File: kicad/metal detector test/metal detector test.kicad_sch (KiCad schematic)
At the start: 107 parts, among them J1 3.5mm audio jack TRS, Q1 PNP, Q2 NPN, SW0 SW_SPST, SW1 SW_SPST, SW2 SW_SPST, SW3 SW_SPST, SW4 SW_SPST, SW5 SW_SPST, SW6 SW_SPST, SW7 SW_SPST, SW8 SW_SPST, SW9 SW_SPST, U1 9v lin reg, U10 3.3v lin reg, U11 lp filter, U12 op amp (lower voltage), U2 op amp (higher voltage), U3 nucleo-32 uC module, U4 5v lin reg, U5 3.3v lin reg, U6 audio amp, U7 lp filter, U8 switch debounce, U9 5v lin reg

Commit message: slow progress
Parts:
- added JP5: SolderJumper_2_Open_big, allen footprints:SolderJumper-2_Open_big_allen, symbol Jumper:SolderJumper_2_Open
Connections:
- net +9V: now also JP5.1 (A); no longer C1.1, R1.1, R2.1, R3.1
- new net: C1.1, JP5.2 (B), R1.1, R2.1, R3.1
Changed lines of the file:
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@@
   (junction (at 30.48 58.42) (diameter 0) (color 0 0 0 0)
   )
+  (junction (at 55.88 20.32) (diameter 0) (color 0 0 0 0)
+  )
   (junction (at 139.7 20.32) (diameter 0) (color 0 0 0 0)
   )
@@
     (stroke (width 0) (type default))
   )
+  (wire (pts (xy 59.69 20.32) (xy 55.88 20.32))
+    (stroke (width 0) (type default))
+  )
   (wire (pts (xy 20.32 78.74) (xy 20.32 81.28))
     (stroke (width 0) (type default))
@@
       (effects (font (size 1.27 1.27)) hide)
     )
-    (property "Datasheet" "https://www.ti.com/lit/gpn/OPA2320" (at 109.22 22.86 0)
+    (property "Datasheet" "https://www.ti.com/lit/ds/symlink/opa2140.pdf?HQS=dis-dk-null-digikeymode-dsf-pf-null-wwe&ts=1680023654676&ref_url=https%253A%252F%252Fwww.ti.com%252Fgeneral%252Fdocs%252Fsuppproductinfo.tsp%253FdistId%253D10%2526gotoUrl%253Dhttps%253A%252F%252Fwww.ti.com%252Flit%252Fgpn%252Fopa2140" (at 109.22 22.86 0)
       (effects (font (size 1.27 1.27)) hide)
     )
@@
       (effects (font (size 1.27 1.27) italic) (justify left) hide)
     )
-    (property "Datasheet" "http://www.st.com/content/ccc/resource/technical/document/datasheet/41/4f/b3/b0/12/d4/47/88/CD00000444.pdf/files/CD00000444.pdf/jcr:content/translations/en.CD00000444.pdf" (at 27.94 110.49 0)
+    (property "Datasheet" "https://www.ti.com/lit/ds/slvs059t/slvs059t.pdf" (at 27.94 110.49 0)
       (effects (font (size 1.27 1.27)) hide)
     )
@@
       (effects (font (size 1.27 1.27)) hide)
     )
-    (property "Datasheet" "https://www.ti.com/lit/gpn/OPA2320" (at 90.17 55.88 0)
+    (property "Datasheet" "https://www.ti.com/lit/ds/symlink/opa2140.pdf?HQS=dis-dk-null-digikeymode-dsf-pf-null-wwe&ts=1680023654676&ref_url=https%253A%252F%252Fwww.ti.com%252Fgeneral%252Fdocs%252Fsuppproductinfo.tsp%253FdistId%253D10%2526gotoUrl%253Dhttps%253A%252F%252Fwww.ti.com%252Flit%252Fgpn%252Fopa2140" (at 90.17 55.88 0)
       (effects (font (size 1.27 1.27)) hide)
     )
@@
     )
   )
-  (symbol (lib_id "power:+9V") (at 45.72 20.32 0) (unit 1)
+  (symbol (lib_id "power:+9V") (at 67.31 20.32 270) (unit 1)
     (in_bom yes) (on_board yes) (dnp no) (fields_autoplaced)
-    (property "Reference" "#PWR01" (at 45.72 24.13 0)
+    (property "Reference" "#PWR01" (at 63.5 20.32 0)
       (effects (font (size 1.27 1.27)) hide)
     )
-    (property "Value" "+9V" (at 45.72 15.24 0)
-      (effects (font (size 1.27 1.27)))
+    (property "Value" "+9V" (at 71.12 20.955 90)
+      (effects (font (size 1.27 1.27)) (justify left))
     )
-    (property "Footprint" "" (at 45.72 20.32 0)
+    (property "Footprint" "" (at 67.31 20.32 0)
       (effects (font (size 1.27 1.27)) hide)
     )
-    (property "Datasheet" "" (at 45.72 20.32 0)
+    (property "Datasheet" "" (at 67.31 20.32 0)
       (effects (font (size 1.27 1.27)) hide)
     )
@@
       (effects (font (size 1.27 1.27) italic) hide)
     )
-    (property "Datasheet" "https://www.analog.com/media/en/technical-documentation/data-sheets/112935ff.pdf" (at 152.4 21.59 0)
+    (property "Datasheet" "https://www.ti.com/lit/ds/symlink/lm2940-n.pdf?HQS=dis-dk-null-digikeymode-dsf-pf-null-wwe&ts=1680023082050&ref_url=https%253A%252F%252Fwww.ti.com%252Fgeneral%252Fdocs%252Fsuppproductinfo.tsp%253FdistId%253D10%2526gotoUrl%253Dhttps%253A%252F%252Fwww.ti.com%252Flit%252Fgpn%252Flm2940-n" (at 152.4 21.59 0)
       (effects (font (size 1.27 1.27)) hide)
     )
@@
     )
   )
+  (symbol (lib_id "Jumper:SolderJumper_2_Open") (at 63.5 20.32 180) (unit 1)
+    (in_bom yes) (on_board yes) (dnp no) (fields_autoplaced)
+    (property "Reference" "JP5" (at 63.5 15.24 0)
+      (effects (font (size 1.27 1.27)))
+    )
+    (property "Value" "SolderJumper_2_Open_big" (at 63.5 17.78 0)
+      (effects (font (size 1.27 1.27)))
+    )
+    (property "Footprint" "allen footprints:SolderJumper-2_Open_big_allen" (at 63.5 20.32 0)
+      (effects (font (size 1.27 1.27)) hide)
+    )
+    (property "Datasheet" "~" (at 63.5 20.32 0)
+      (effects (font (size 1.27 1.27)) hide)
+    )
+    (property "MPN" "" (at 63.5 20.32 0)
+      (effects (font (size 1.27 1.27)) hide)
+    )
+    (pin "1")
+    (pin "2")
+    (instances
+      (project "metal detector test"
+        (path "/aac94249-970f-41d5-8c24-6bade512464d"
+          (reference "JP5") (unit 1)
+        )
+      )
+    )
+  )
   (symbol (lib_id "power:GNDPWR") (at 139.7 25.4 0) (unit 1)
     (in_bom yes) (on_board yes) (dnp no)
@@
       (effects (font (size 1.27 1.27)) hide)
     )
-    (property "Datasheet" "https://www.ti.com/lit/gpn/OPA2320" (at 90.17 55.88 0)
+    (property "Datasheet" "https://www.ti.com/lit/ds/symlink/opa2140.pdf?HQS=dis-dk-null-digikeymode-dsf-pf-null-wwe&ts=1680023654676&ref_url=https%253A%252F%252Fwww.ti.com%252Fgeneral%252Fdocs%252Fsuppproductinfo.tsp%253FdistId%253D10%2526gotoUrl%253Dhttps%253A%252F%252Fwww.ti.com%252Flit%252Fgpn%252Fopa2140" (at 90.17 55.88 0)
       (effects (font (size 1.27 1.27)) hide)
     )
@@
       (effects (font (size 1.27 1.27) italic) (justify left) hide)
     )
-    (property "Datasheet" "http://www.st.com/content/ccc/resource/technical/document/datasheet/41/4f/b3/b0/12/d4/47/88/CD00000444.pdf/files/CD00000444.pdf/jcr:content/translations/en.CD00000444.pdf" (at 27.94 74.93 0)
+    (property "Datasheet" "https://www.ti.com/lit/ds/slvs059t/slvs059t.pdf" (at 27.94 74.93 0)
       (effects (font (size 1.27 1.27)) hide)
     )

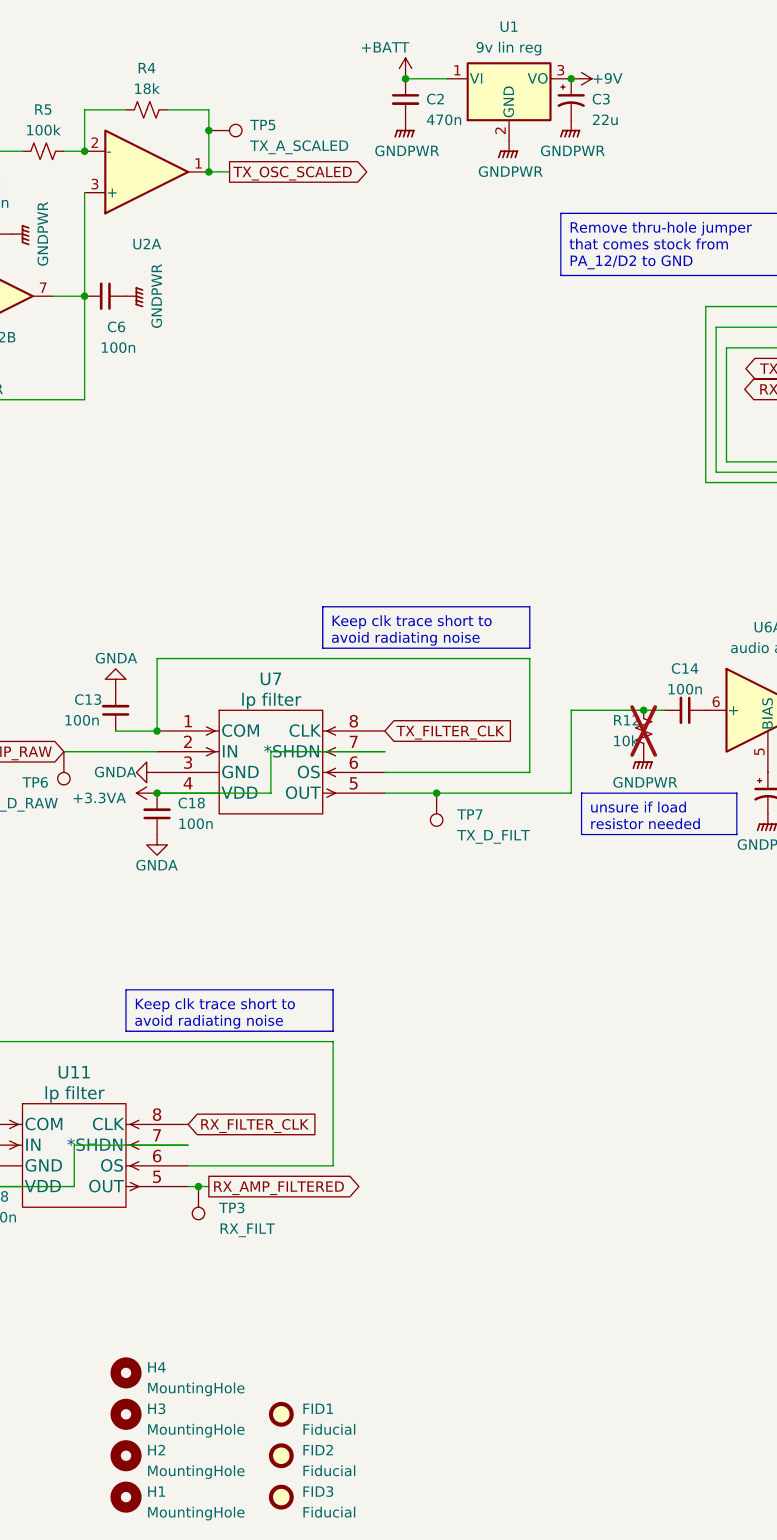
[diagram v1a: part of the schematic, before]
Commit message: Added holes on corners of OLED footprint after carefully measuring twice, working on layout still.
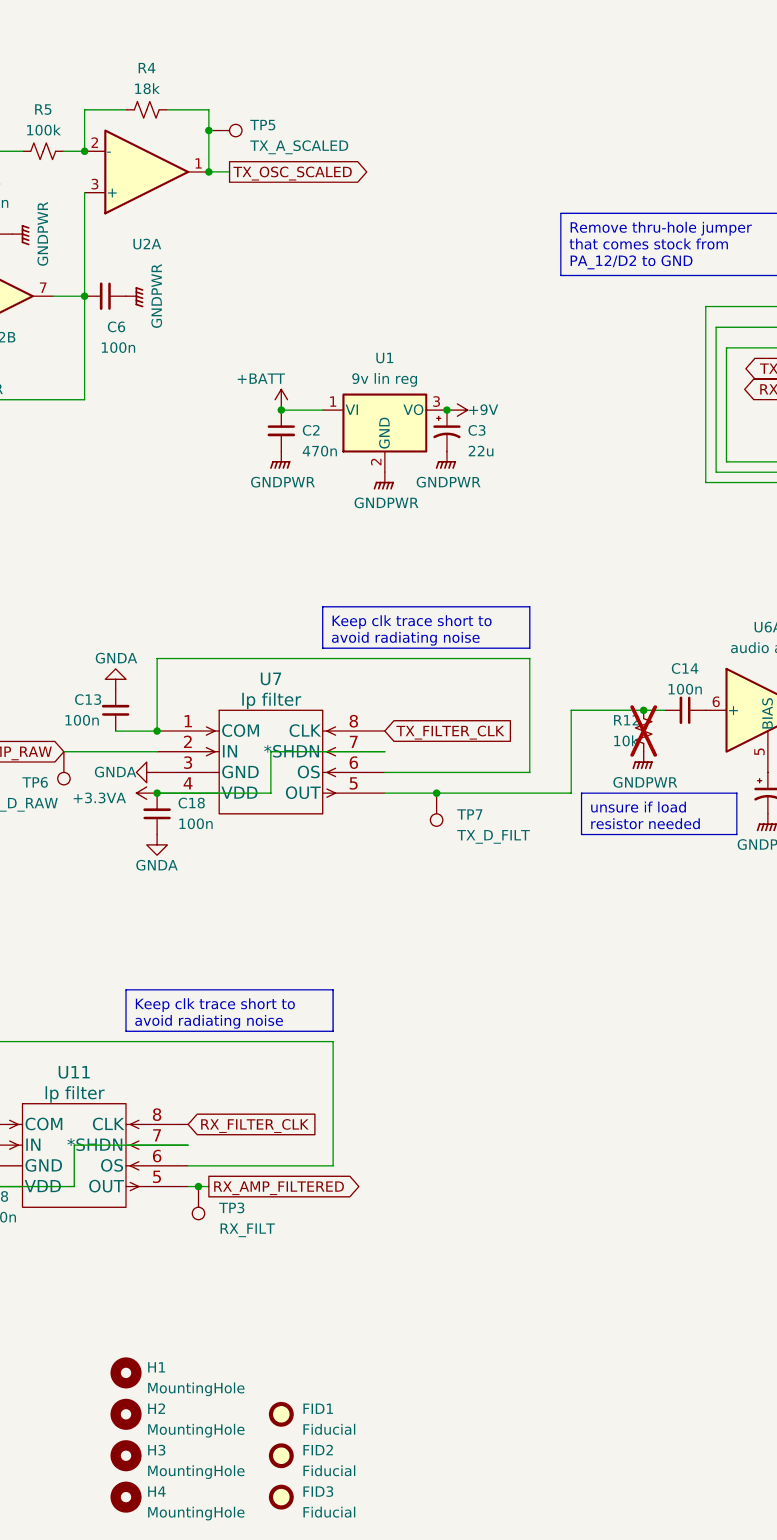
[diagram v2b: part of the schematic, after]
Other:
- moved on the sheet: C2, C3, H1, H2, H3, H4, U1

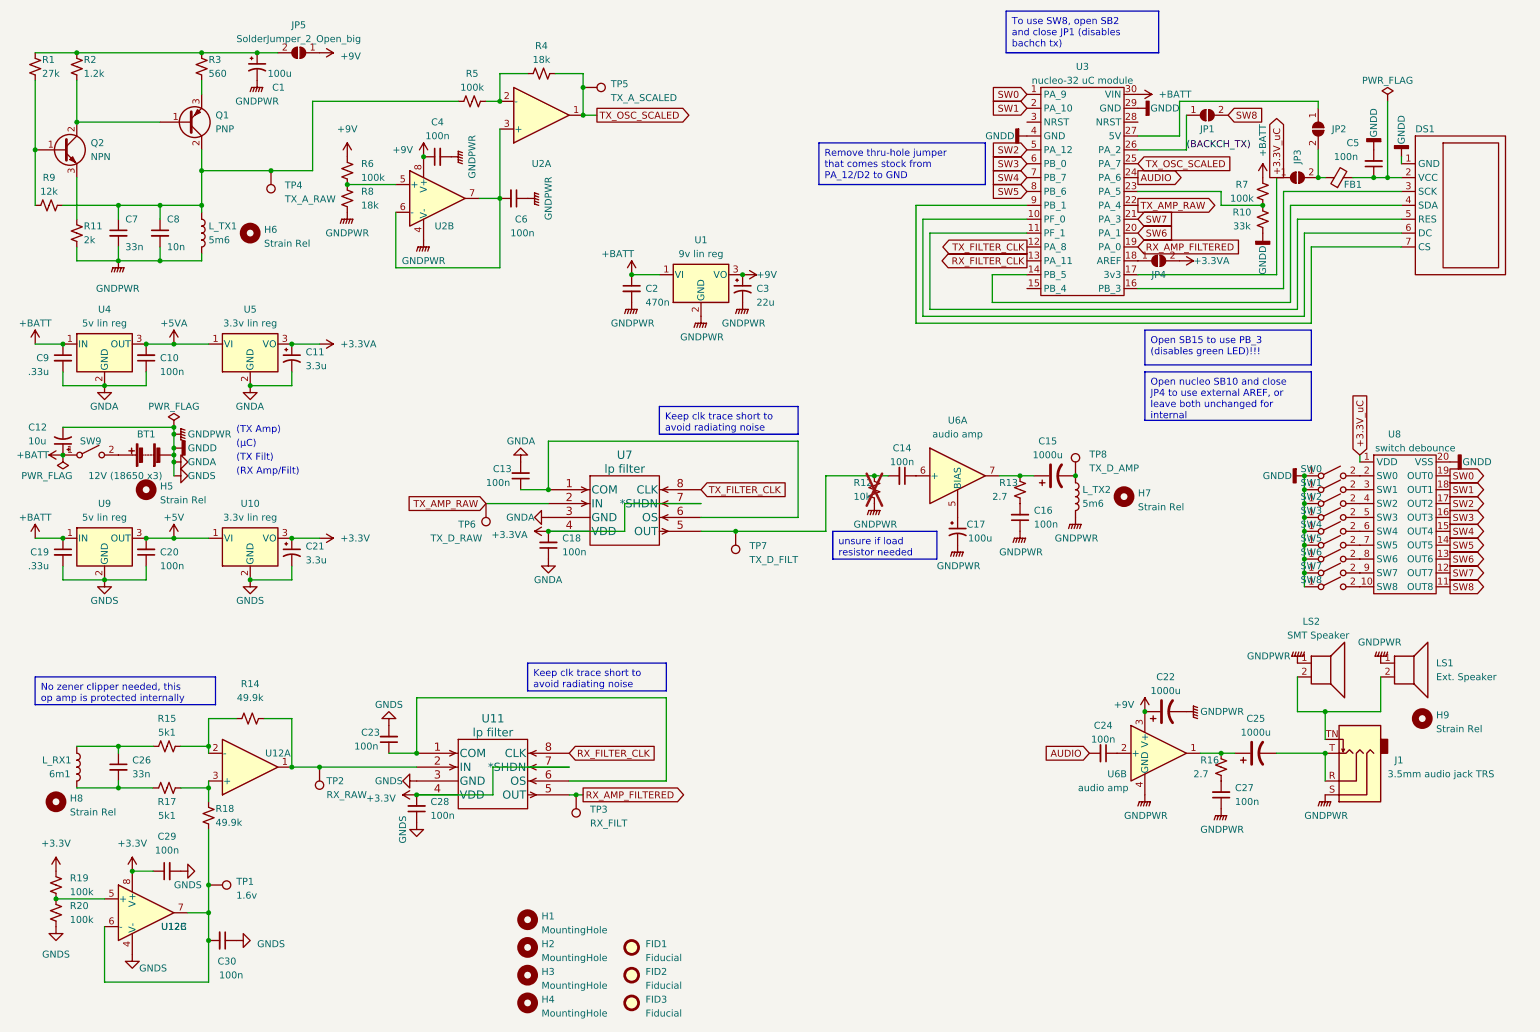
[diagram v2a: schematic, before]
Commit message: Making custom mounting / strain relief holes
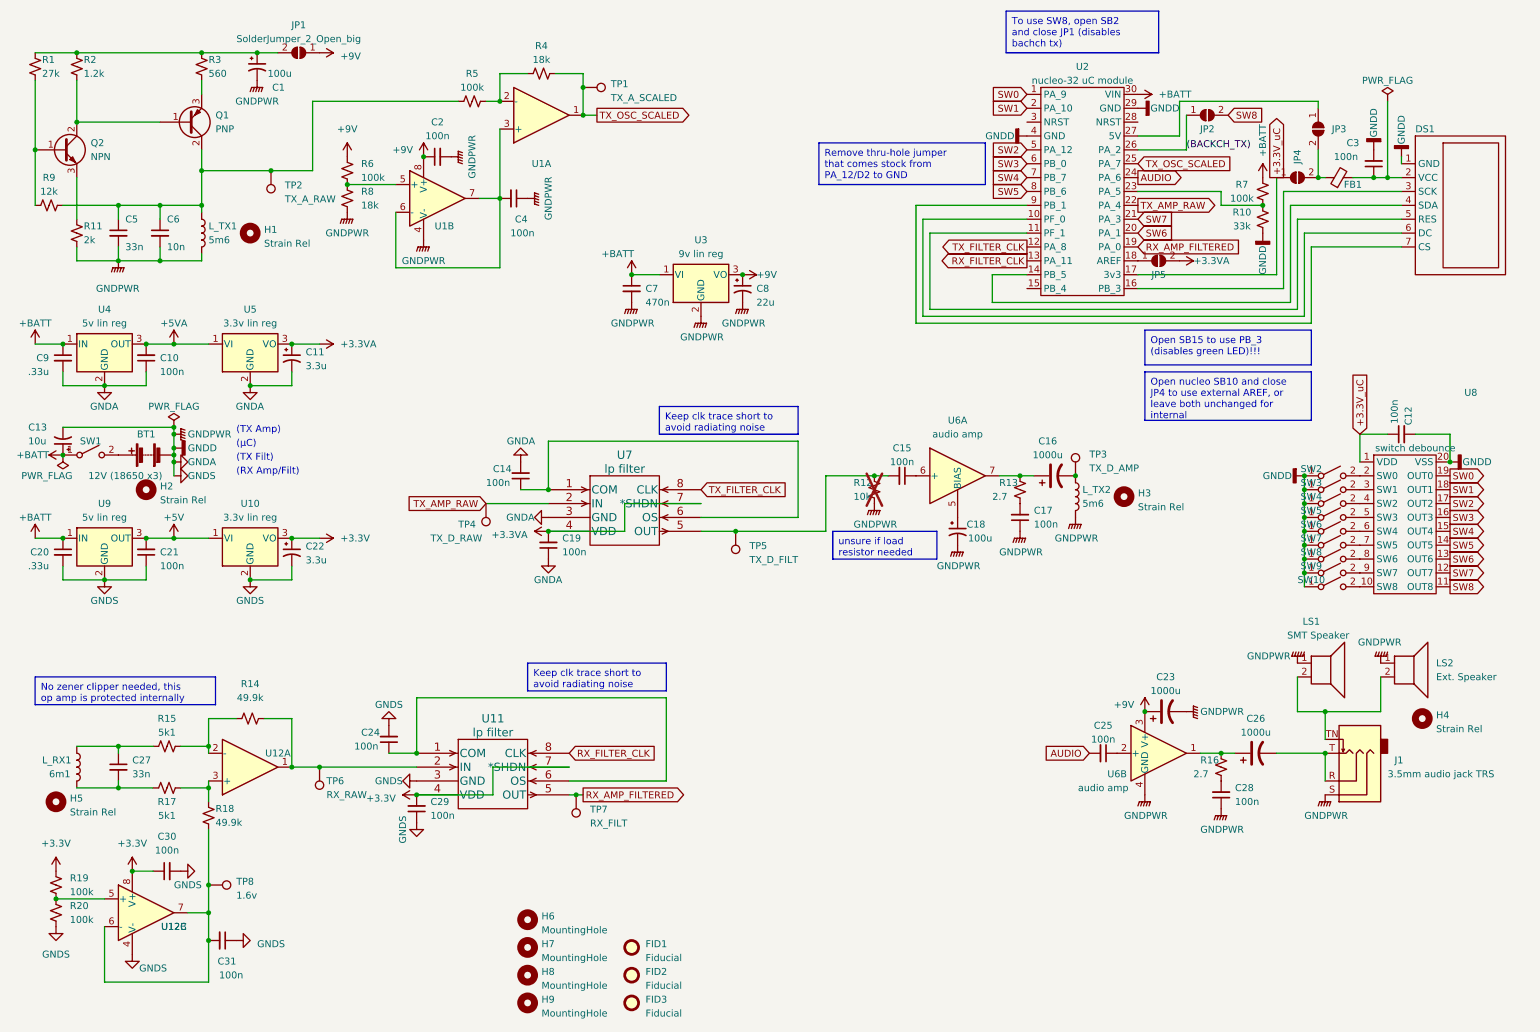
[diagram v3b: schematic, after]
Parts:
- removed H2, H3, H4: MountingHole, MountingHole:MountingHole_3.7mm, symbol Mechanical:MountingHole
- added C12: 100n, Capacitor_SMD:C_0805_2012Metric_Pad1.18x1.45mm_HandSolder, symbol Device:C_Small
- added H7, H8, H9: MountingHole, allen footprints:mounting_hole_4-40_thru, symbol Mechanical:MountingHole
- H1: renamed from H6; footprint MountingHole:MountingHole_3.2mm_M3 -> allen footprints:mounting_hole_3mm
- H2: renamed from H5; footprint MountingHole:MountingHole_3.2mm_M3 -> allen footprints:mounting_hole_3mm
- H3: renamed from H7; footprint MountingHole:MountingHole_3.2mm_M3 -> allen footprints:mounting_hole_3mm
- H4: renamed from H9; footprint MountingHole:MountingHole_3.2mm_M3 -> allen footprints:mounting_hole_3mm
- H5: renamed from H8; footprint MountingHole:MountingHole_3.2mm_M3 -> allen footprints:mounting_hole_3mm
- H6: renamed from H1; footprint MountingHole:MountingHole_3.7mm -> allen footprints:mounting_hole_4-40_thru
- renumbered C12 to C13, C13 to C14, C14 to C15, C15 to C16, C16 to C17, C17 to C18, C18 to C19, C4 to C2, C19 to C20, C20 to C21, C21 to C22, C22 to C23, C23 to C24, C24 to C25, C25 to C26, C26 to C27, C27 to C28, C28 to C29, C5 to C3, C29 to C30, C30 to C31, C6 to C4, C7 to C5, C8 to C6, C2 to C7, C3 to C8, JP5 to JP1, JP1 to JP2, JP2 to JP3, JP3 to JP4, JP4 to JP5, LS2 to LS1, LS1 to LS2, SW9 to SW1, SW8 to SW10, SW0 to SW2, SW1 to SW3, SW2 to SW4, SW3 to SW5, SW4 to SW6, SW5 to SW7, SW6 to SW8, SW7 to SW9, TP5 to TP1, TP4 to TP2, TP8 to TP3, TP6 to TP4, TP7 to TP5, TP2 to TP6, TP3 to TP7, TP1 to TP8, U2 to U1, U3 to U2, U1 to U3
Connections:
- net +3.3V_uC: now also C12.1
- net GNDA: now also C12.2

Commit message: making progress on pcb layout
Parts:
- renumbered C23 to C12, C12 to C13, C13 to C14, C14 to C15, C15 to C16, C16 to C17, C17 to C18, C24 to C23, C25 to C24, C26 to C25, C27 to C26, C28 to C27, C29 to C28, C18 to C29
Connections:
- net +BATT: now also SW1.2 (B); no longer SW1.1 (A)
- net GNDA: now also LS1.2; no longer LS1.1
- net at BT1.1 (+): now also SW1.1 (A); no longer SW1.2 (B)
- net at C16.1: now also U6.2 (+); no longer U6.6 (+)
- net at C25.1, R16.1: now also U6.7; no longer U6.1
- net at C24.1: now also U6.6 (+); no longer U6.2 (+)
- net at C17.1, R13.1: now also U6.1; no longer U6.7
- net at J1.TN, LS2.2: now also LS1.1; no longer LS1.2
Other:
- moved on the sheet: C12, C29, LS1, SW1, U6A, U6B
